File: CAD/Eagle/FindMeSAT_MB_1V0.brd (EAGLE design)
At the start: 99 x 49.2 mm, 107 parts, among them IC1111 LM2831YMF, J291 MCX-J-P-X-RA-SM1, J701 MOLEX_105017-0001, J801 MICROSIM-8P_SDCARD-8P_MOLEX-1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, J901 JST_S3B-XH-A, Q101 ABS07, U1001 CFPT-141, U101 ATXMEGA256A3BU-AU, U1011 OPA354, U1021 OPA354, U1121 LM4120IM5-3.0, U201 SIM808

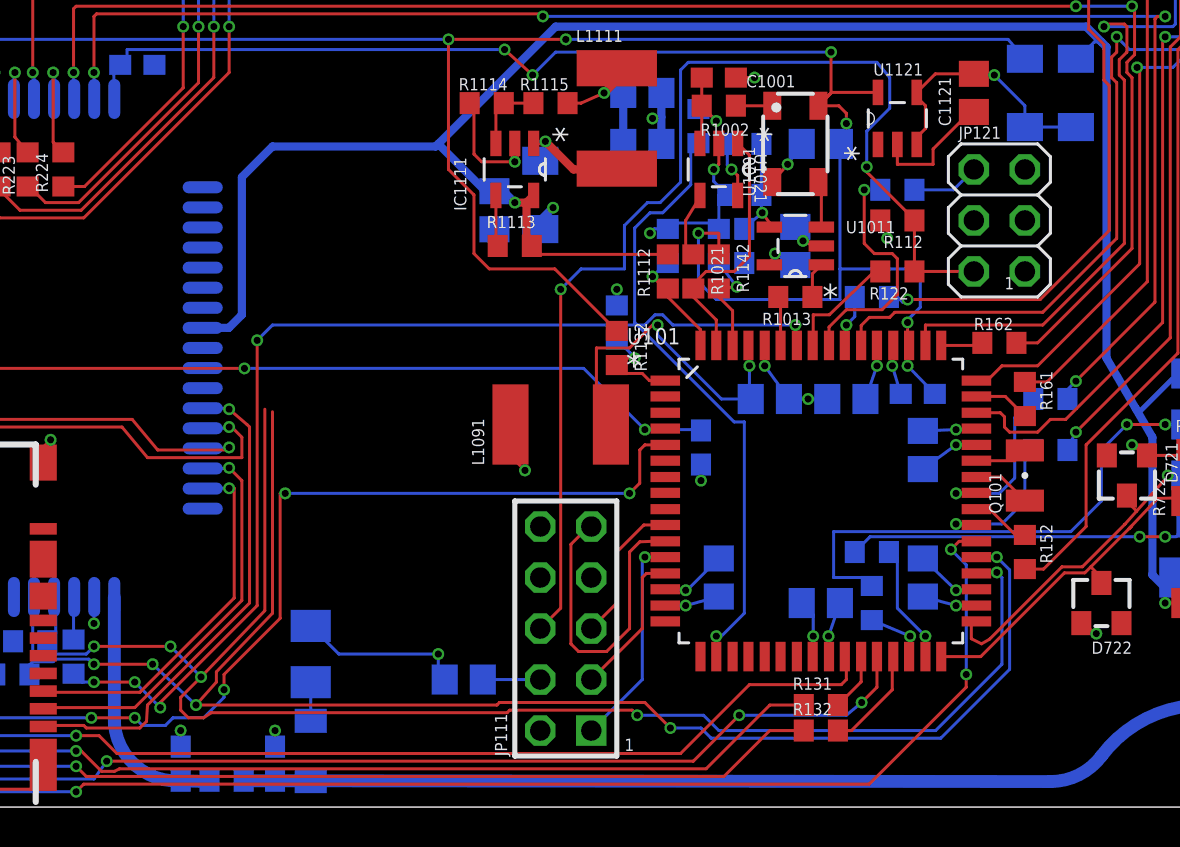
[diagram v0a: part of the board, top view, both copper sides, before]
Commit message: Eagle - missing Display header added
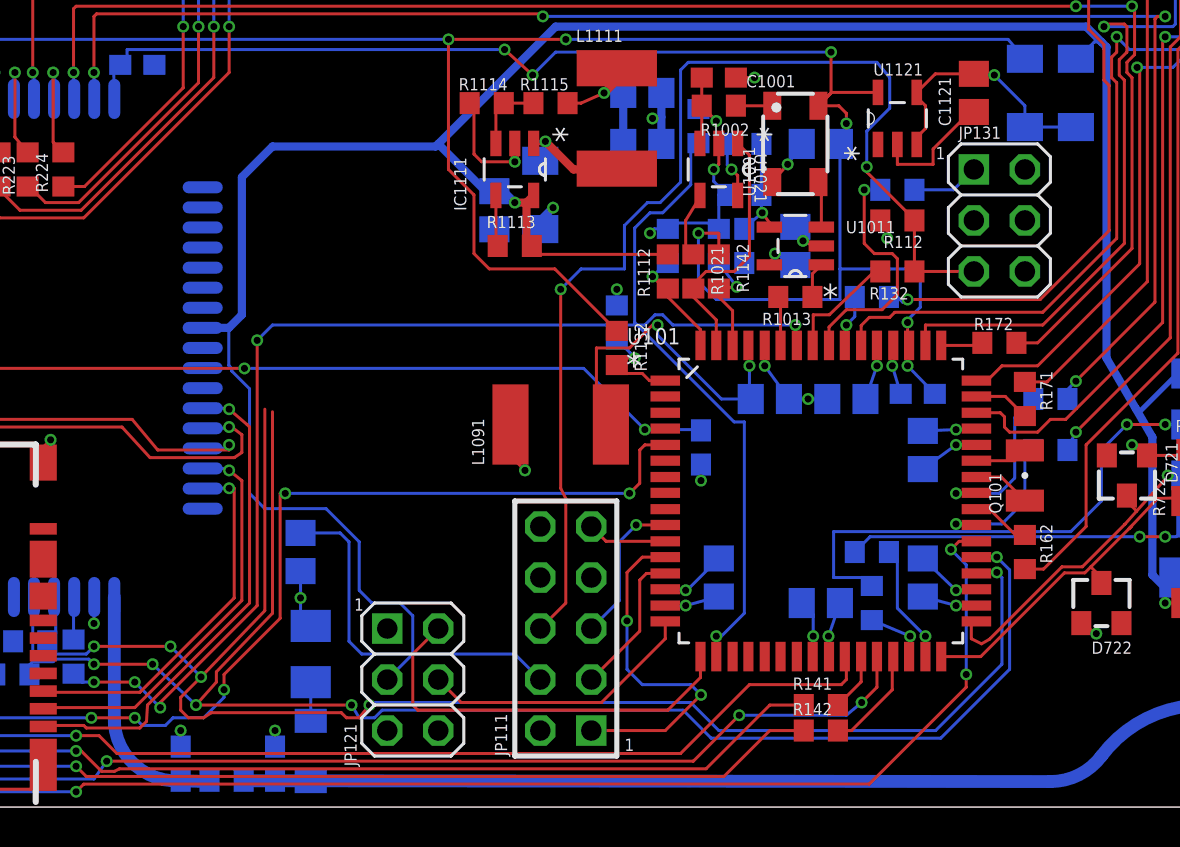
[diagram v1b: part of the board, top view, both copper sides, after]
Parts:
- removed R121, R122, R153: 27, rcl:R0603
- added JP131: PDI, df4iah_connector:2X03
- added R171, R172, R173: 27, rcl:R0603
- JP121: value PDI -> DISPLAY
- R151: value 4.7k -> 27
- R161: value 27 -> 4.7k
- moved JP121 37.1 mm to (52.1, 6.35)
- moved R131 25.9 mm to (76.2, 30.7), flipped to the bottom, turned to 0 degrees
- moved R132 23.2 mm to (76.2, 26.7)
- moved R151 11.7 mm to (74.9, 10.2), turned to 90 degrees
- moved R162 10.5 mm to (82.5, 12.7), turned to 270 degrees
- moved R111 10.3 mm to (46.5, 12.7), turned to 270 degrees
- moved R163 10.2 mm to (83.8, 20.3)
- moved R142 9.25 mm to (72.4, 3.81), flipped to the top, turned to 180 degrees
- moved R152 7.62 mm to (74.9, 12.7), flipped to the bottom, turned to 0 degrees
- moved R141 5.68 mm to (72.4, 5.08), flipped to the top, turned to 180 degrees
- moved R161 2.84 mm to (83.8, 17.8), flipped to the bottom, turned to 180 degrees
- renumbered C131 to C141, C151 to C101
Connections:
- new net AD_PHS_I: U101.2
- new net AD_PHS_Q: U101.3
- new net PULSE_I: U101.20
- new net PULSE_Q: U101.21
- new net SCL2: JP121.2, U101.17
- new net SDA2: JP121.4, U101.16
- net +3V3: now also JP121.5, JP131.2; no longer JP121.2
- net +5V: now also JP121.3
- net CTS1: now also R173.1; no longer R163.1
- net DCD1: now also R171.1; no longer R161.1
- net GND: now also JP121.1, JP131.6
- net GSM_DTR: now also R171.2; no longer R161.2
- net GSM_PCM_CLK: now also R141.2; no longer R131.2
- net GSM_PCM_CLK_DRV: now also R141.1; no longer R131.1
- net GSM_PCM_IN: now also R142.2; no longer R132.2
- net GSM_PCM_IN_DRV: now also R142.1; no longer R132.1
- net GSM_PWRKEY: now also R162.2; no longer R152.2
- net GSM_RESET: now also R163.2; no longer R153.2
- net GSM_RTS: now also R173.2; no longer R163.2
- net GSM_RXD: now also R172.2; no longer R162.2
- net GSM_VDD_EXT: now also R161.2; no longer R151.2
- net PDI_CLK: now also JP131.5, R132.1; no longer JP121.5, R122.1
- net PDI_CLK_CPU: now also R132.2; no longer R122.2
- net PDI_DATA: now also JP131.1, R131.1; no longer JP121.1, R121.1
- net PDI_DATA_CPU: now also R131.2; no longer R121.2
- net POWERED_GSM: now also R161.1; no longer R151.1
- net PWRKEY_GSM: now also R162.1; no longer R152.1
- net RESET_GSM: now also R163.1; no longer R153.1
- net TXD1: now also R172.1; no longer R162.1
- net USB_ID: now also R151.2; no longer R141.2
- net USB_ID_DRV: now also R151.1; no longer R141.1
- net USB_RESET: now also R152.2; no longer R142.2
- net USB_RESET_DRV: now also R152.1; no longer R142.1
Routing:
- net +5V: track 106.4 -> 130.8 mm
- net SCL2: track 0.00 -> 20.5 mm
- net VREF: track 2.86 -> 17.9 mm
- net SDA2: track 0.00 -> 14.0 mm
- net TDI: track 15.7 -> 4.12 mm
- net TCK: track 10.8 -> 17.5 mm, vias 1 -> 2
- net +3V3: track 37.7 -> 33.2 mm
- net SDA1: track 76.6 -> 77.3 mm
- net TMS: track 7.31 -> 7.78 mm, vias 0 -> 1

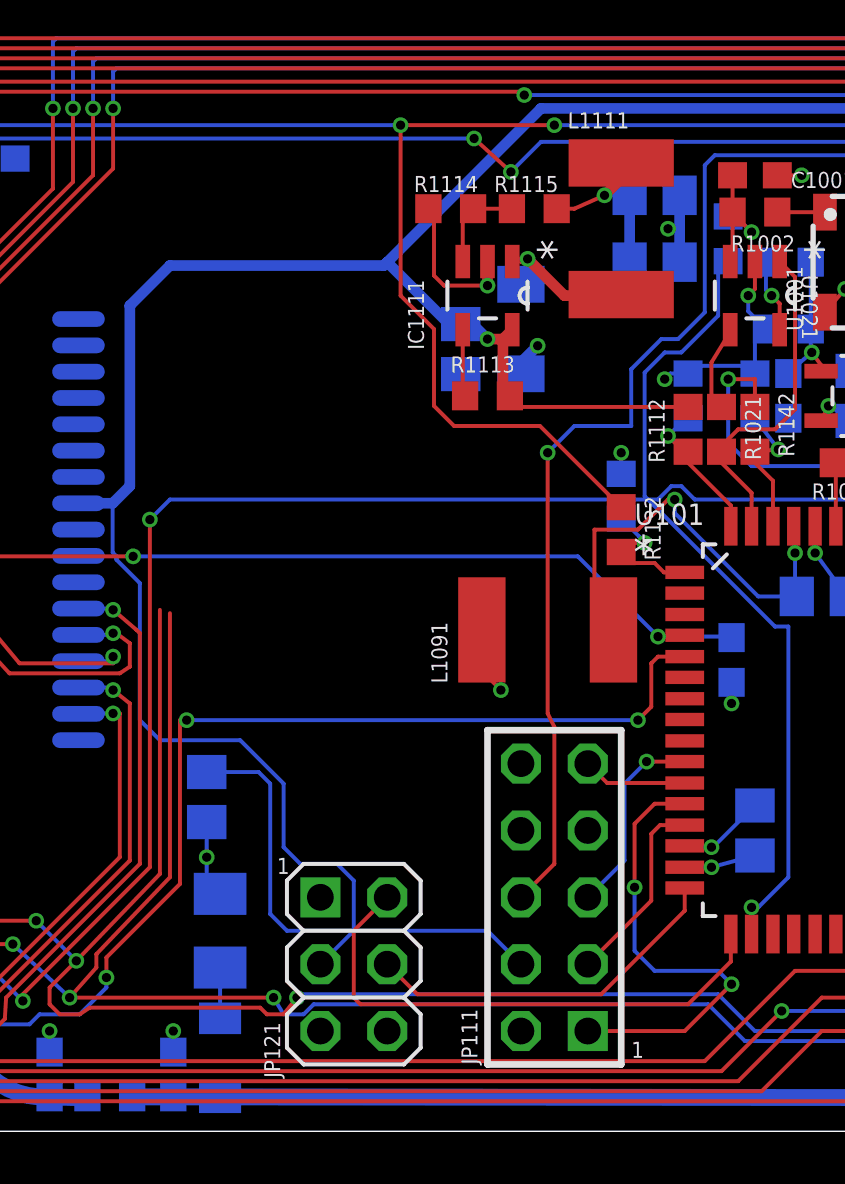
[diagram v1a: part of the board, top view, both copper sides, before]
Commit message: Eagle - additional sensors added (9-axis: accel / gyro / magneto, baro, hygro)
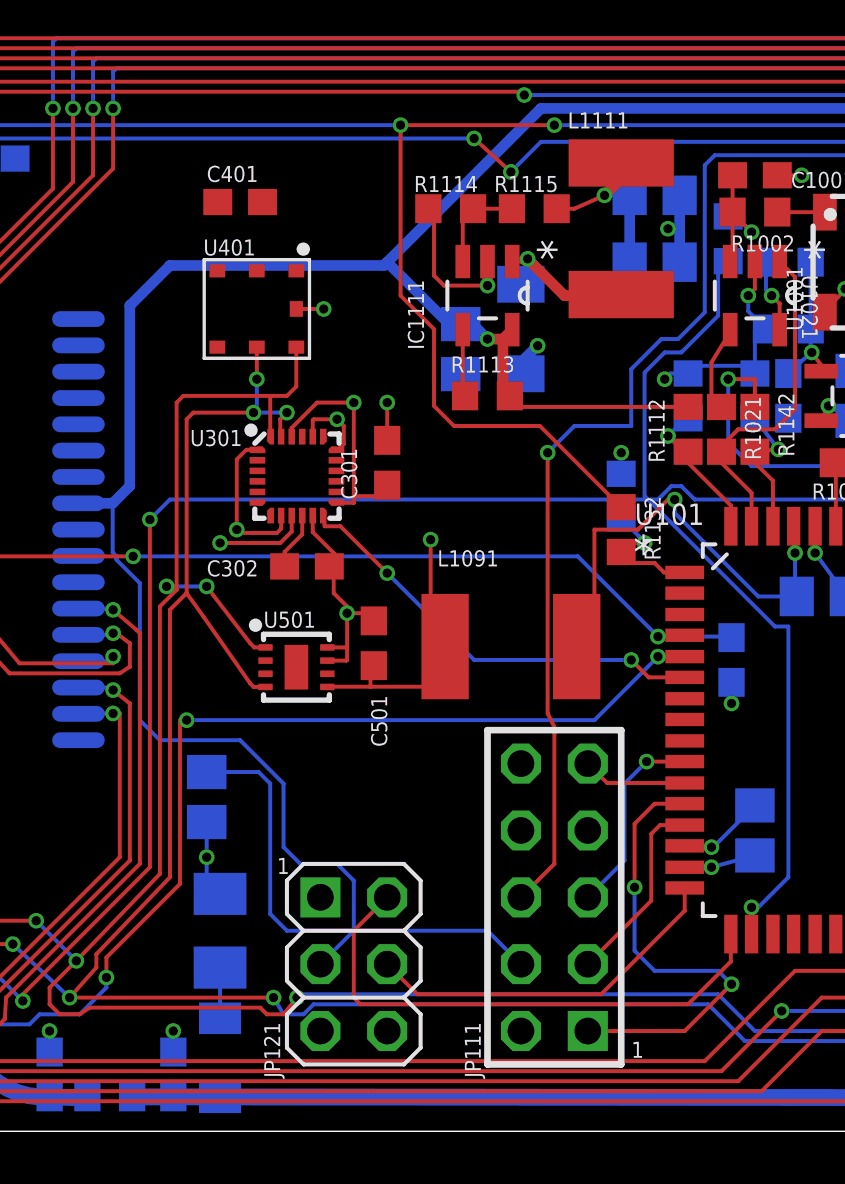
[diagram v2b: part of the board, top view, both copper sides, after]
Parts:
- added C301, C302, C401, C501: 100n, rcl:C0603
- added U301: MPU-9250, df4iah_sensors:QFN24-3X3
- added U401: BMP180, df4iah_sensors:BMP180
- added U501: SHT31-DIS, df4iah_sensors:DFN8/SHT
- U101: device df4iah_mmu:QFP80P1600X1600X120-64N -> df4iah_processors:QFP80P1600X1600X120-64N
- U201: device adafruit:SIM900_SMT -> df4iah_processors:SIM808
- moved L1091 1.53 mm to (58.0, 18.4)
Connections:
- new net GAM_RO: C302.1, U301.10
- new net I2C2_INT: U101.6, U301.12
- net +3V3: now also C301.1, C401.1, C501.1, U301.1, U301.13, U301.22, U301.8, U401.2, U401.3, U501.5
- net GND: now also C301.2, C302.2, C401.2, C501.2, U301.11, U301.18, U301.20, U301.9, U401.7, U501.2, U501.7, U501.8, U501.9
- net PULSE_I: now also U101.19; no longer U101.20
- net PULSE_Q: now also U101.20; no longer U101.21
- net SCL1: now also U301.23, U401.5, U501.4
- net SDA1: now also U301.24, U401.6, U501.1
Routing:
- net SDA1: track 77.3 -> 98.5 mm, vias 5 -> 7
- net +3V3: track 33.2 -> 54.3 mm, vias 11 -> 13
- net SCL1: track 79.1 -> 99.1 mm, vias 5 -> 8
- net GND: track 150.5 -> 168.3 mm, vias 42 -> 47
- net I2C2_INT: track 0.00 -> 16.4 mm, vias 0 -> 2
- net GAM_RO: track 0.00 -> 2.21 mm
- net GSM_NETLIGHT: track 57.0 -> 56.0 mm
